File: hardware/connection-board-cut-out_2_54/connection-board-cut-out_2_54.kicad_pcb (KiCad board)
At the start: 2 copper layers, 175 x 90 mm, 28 parts

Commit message: docs(hardware): label pcb variants on silkscreen
Add clear variant labels to the board version line so the two
connector board variants can be identified directly on the PCB.

Made-with: Cursor
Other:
- board text added: "Open Locker Connector Board Version: 1.1.0 (JST-XH 2.54 mm) Power supply: 12V Bus: Modbus RTU Docs: https://github.com/Open-Locker/Open-Locker Designed for: https://www.waveshare.com/wiki/Modbus_RTU_Relay_(D)"
- board text removed: "Open Locker Connector Board Version: 1.1.0 Power supply: 12V Bus: Modbus RTU Docs: https://github.com/Open-Locker/Open-Locker Designed for: https://www.waveshare.com/wiki/Modbus_RTU_Relay_(D)"
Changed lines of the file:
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@@
 		)
 	)
-	(gr_text "Open Locker Connector Board\n\nVersion: 1.1.0\n\nPower supply: 12V\nBus: Modbus RTU\n\nDocs: https://github.com/Open-Locker/Open-Locker\nDesigned for: https://www.waveshare.com/wiki/Modbus_RTU_Relay_(D)"
+	(gr_text "Open Locker Connector Board\n\nVersion: 1.1.0 (JST-XH 2.54 mm)\n\nPower supply: 12V\nBus: Modbus RTU\n\nDocs: https://github.com/Open-Locker/Open-Locker\nDesigned for: https://www.waveshare.com/wiki/Modbus_RTU_Relay_(D)"
 		(at 219 122 90)
 		(layer "F.SilkS")

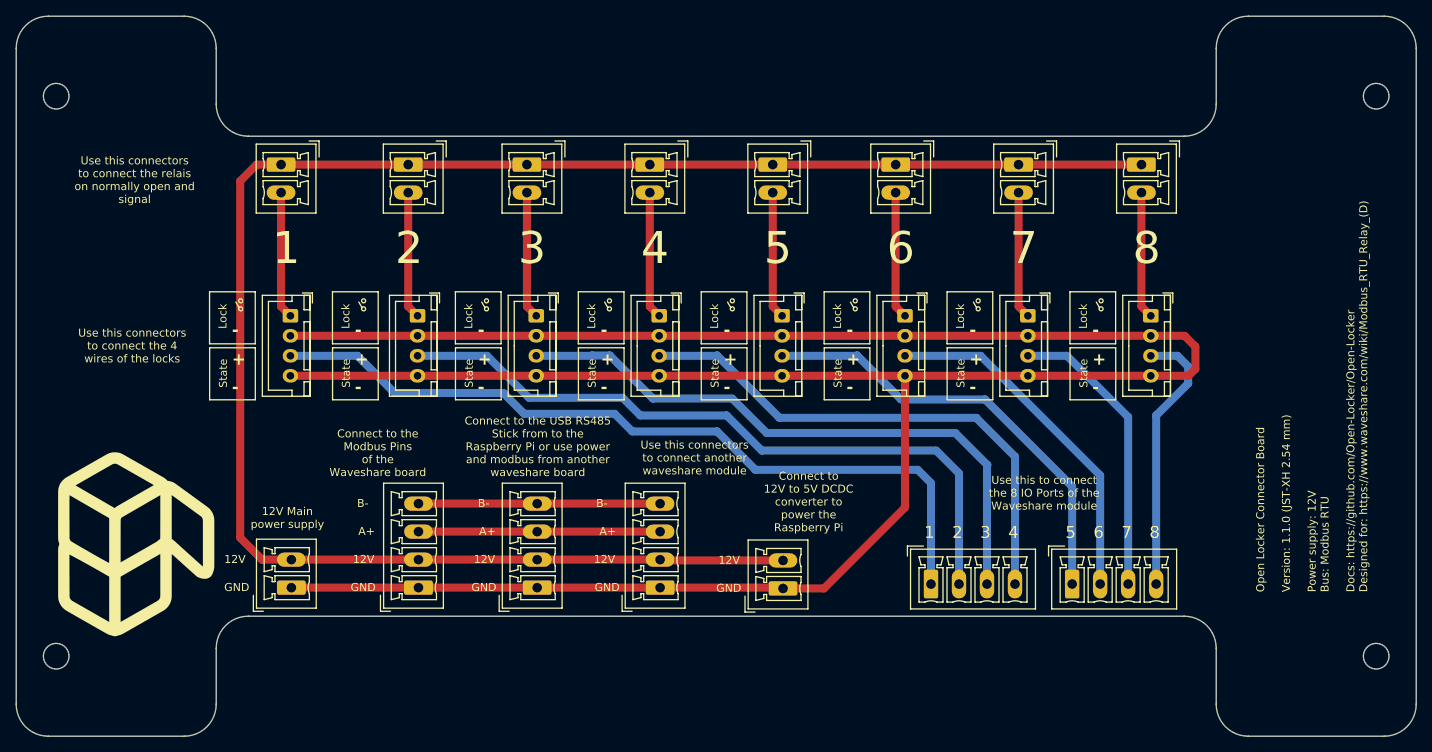
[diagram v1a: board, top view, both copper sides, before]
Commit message: add 1N4007 diode between power supply and coil
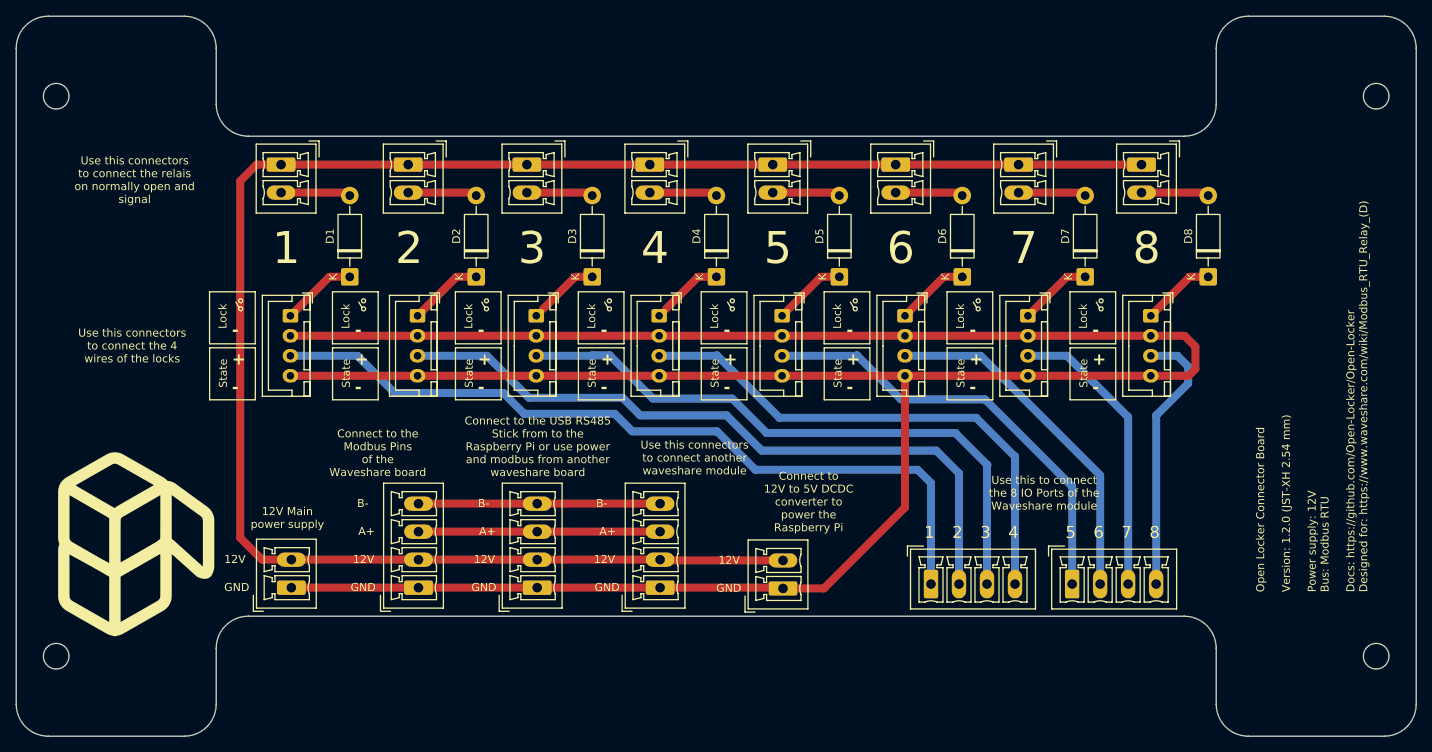
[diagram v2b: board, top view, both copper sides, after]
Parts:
- added D1: 1N4007, Diode_THT:D_DO-41_SOD81_P10.16mm_Horizontal, F.Cu at (91.7, 82.6)
- added D2: 1N4007, Diode_THT:D_DO-41_SOD81_P10.16mm_Horizontal, F.Cu at (107.5, 82.6)
- added D3: 1N4007, Diode_THT:D_DO-41_SOD81_P10.16mm_Horizontal, F.Cu at (122.0, 82.6)
- added D4: 1N4007, Diode_THT:D_DO-41_SOD81_P10.16mm_Horizontal, F.Cu at (137.5, 82.6)
- added D5: 1N4007, Diode_THT:D_DO-41_SOD81_P10.16mm_Horizontal, F.Cu at (152.9, 82.6)
- added D6: 1N4007, Diode_THT:D_DO-41_SOD81_P10.16mm_Horizontal, F.Cu at (168.3, 82.6)
- added D7: 1N4007, Diode_THT:D_DO-41_SOD81_P10.16mm_Horizontal, F.Cu at (183.6, 82.6)
- added D8: 1N4007, Diode_THT:D_DO-41_SOD81_P10.16mm_Horizontal, F.Cu at (199.0, 82.6)
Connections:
- LOCK_1 pad 1: Net-(CH_1-Pin_2) -> Net-(D1-K)
- LOCK_2 pad 1: Net-(CH_2-Pin_2) -> Net-(D2-K)
- LOCK_3 pad 1: Net-(CH_3-Pin_2) -> Net-(D3-K)
- LOCK_4 pad 1: Net-(CH_4-Pin_2) -> Net-(D4-K)
- LOCK_5 pad 1: Net-(CH_5-Pin_2) -> Net-(D5-K)
- LOCK_6 pad 1: Net-(CH_6-Pin_2) -> Net-(D6-K)
- LOCK_7 pad 1: Net-(CH_7-Pin_2) -> Net-(D7-K)
- LOCK_8 pad 1: Net-(CH_8-Pin_2) -> Net-(D8-K)
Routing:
- net Net-(D1-K): track 0.00 -> 9.44 mm
- net Net-(D2-K): track 0.00 -> 9.35 mm
- net Net-(D8-K): track 0.00 -> 9.19 mm
- net Net-(D7-K): track 0.00 -> 9.17 mm
- net Net-(D6-K): track 0.00 -> 9.17 mm
- net Net-(D5-K): track 0.00 -> 9.17 mm
- net Net-(D4-K): track 0.00 -> 7.97 mm
- net Net-(D3-K): track 0.00 -> 7.81 mm
- net Net-(CH_3-Pin_2): track 15.9 -> 8.31 mm
- net Net-(CH_6-Pin_2): track 15.9 -> 8.48 mm
- net Net-(CH_5-Pin_2): track 15.9 -> 8.48 mm
- net Net-(CH_4-Pin_2): track 15.9 -> 8.48 mm
- net Net-(CH_7-Pin_2): track 15.9 -> 8.48 mm
- net Net-(CH_8-Pin_2): track 15.9 -> 8.49 mm
- net Net-(CH_2-Pin_2): track 15.9 -> 8.65 mm
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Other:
- board text added: "Open Locker Connector Board Version: 1.2.0 (JST-XH 2.54 mm) Power supply: 12V Bus: Modbus RTU Docs: https://github.com/Open-Locker/Open-Locker Designed for: https://www.waveshare.com/wiki/Modbus_RTU_Relay_(D)"
- board text removed: "Open Locker Connector Board Version: 1.1.0 (JST-XH 2.54 mm) Power supply: 12V Bus: Modbus RTU Docs: https://github.com/Open-Locker/Open-Locker Designed for: https://www.waveshare.com/wiki/Modbus_RTU_Relay_(D)"
